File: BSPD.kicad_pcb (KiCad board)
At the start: 2 copper layers, 78.7 x 83 mm, 46 parts, among them J1 Screw_Terminal_3.5mm_2, J2 Screw_Terminal_3.5mm_2, J3 Screw_Terminal_3.5mm_3, J4 Screw_Terminal_3.5mm_3, J5 Screw_Terminal_3.5mm_2, J6 Screw_Terminal_3.5mm_2, J7 Screw_Terminal_3.5mm_2, Q3 NPN, U1 LM358, U2 LM358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

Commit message: Text Added
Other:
- board text added: "BSPD MAMUN_DAQ"
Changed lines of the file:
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@@
 		(layer "Edge.Cuts")
+	)
+	(gr_text "BSPD\nMAMUN_DAQ"
+		(at 186.5 122 0)
+		(layer "B.Cu")
+		(effects
+			(font
+				(size 1.5 1.5)
+				(thickness 0.3)
+				(bold yes)
+			)
+			(justify left bottom mirror)
+		)
 	)
 	(via

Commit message: Rounded PCB
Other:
- board size 78.7 x 83 mm -> 80.9 x 85 mm
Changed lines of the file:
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@@
 		(embedded_fonts no)
 	)
-	(gr_rect
-		(start 115.345 45)
-		(end 194 128)
+	(gr_line
+		(start 126.07107 43)
+		(end 186.92893 43)
 		(stroke
 			(width 0.05)
 			(type default)
 		)
-		(fill no)
 		(layer "Edge.Cuts")
 	)
+	(gr_arc
+		(start 116.071068 53)
+		(mid 119.000001 45.928931)
+		(end 126.07107 43)
+		(stroke
+			(width 0.05)
+			(type default)
+		)
+		(layer "Edge.Cuts")
+	)
+	(gr_arc
+		(start 126 128)
+		(mid 118.928932 125.071068)
+		(end 116 118)
+		(stroke
+			(width 0.05)
+			(type default)
+		)
+		(layer "Edge.Cuts")
+	)
+	(gr_line
+		(start 116 118)
+		(end 116.071068 53)
+		(stroke
+			(width 0.05)
+			(type default)
+		)
+		(layer "Edge.Cuts")
+	)
+	(gr_arc
+		(start 196.928932 117.928932)
+		(mid 194 125)
+		(end 186.928932 127.928932)
+		(stroke
+			(width 0.05)
+			(type default)
+		)
+		(layer "Edge.Cuts")
+	)
+	(gr_line
+		(start 186.928932 127.928932)
+		(end 126 128)
+		(stroke
+			(width 0.05)
+			(type default)
+		)
+		(layer "Edge.Cuts")
+	)
+	(gr_line
+		(start 196.928932 53)
+		(end 196.928932 118)
+		(stroke
+			(width 0.05)
+			(type default)
+		)
+		(layer "Edge.Cuts")
+	)
+	(gr_arc
+		(start 186.928932 43)
+		(mid 194 45.928932)
+		(end 196.928932 53)
+		(stroke
+			(width 0.05)
+			(type default)
+		)
+		(layer "Edge.Cuts")
+	)

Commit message: Final Commit for print
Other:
- board size 80.9 x 85 mm -> 78 x 86 mm
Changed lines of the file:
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@@
 		(embedded_fonts no)
 	)
-	(gr_line
-		(start 126.07107 43)
-		(end 186.92893 43)
+	(gr_rect
+		(start 116 43)
+		(end 194 129)
 		(stroke
 			(width 0.05)
 			(type default)
 		)
+		(fill no)
 		(layer "Edge.Cuts")
 	)
-	(gr_arc
-		(start 116.071068 53)
-		(mid 119.000001 45.928931)
-		(end 126.07107 43)
-		(stroke
-			(width 0.05)
-			(type default)
-		)
-		(layer "Edge.Cuts")
-	)
-	(gr_arc
-		(start 126 128)
-		(mid 118.928932 125.071068)
-		(end 116 118)
-		(stroke
-			(width 0.05)
-			(type default)
-		)
-		(layer "Edge.Cuts")
-	)
-	(gr_line
-		(start 116 118)
-		(end 116.071068 53)
-		(stroke
-			(width 0.05)
-			(type default)
-		)
-		(layer "Edge.Cuts")
-	)
-	(gr_arc
-		(start 196.928932 117.928932)
-		(mid 194 125)
-		(end 186.928932 127.928932)
-		(stroke
-			(width 0.05)
-			(type default)
-		)
-		(layer "Edge.Cuts")
-	)
-	(gr_line
-		(start 186.928932 127.928932)
-		(end 126 128)
-		(stroke
-			(width 0.05)
-			(type default)
-		)
-		(layer "Edge.Cuts")
-	)
-	(gr_line
-		(start 196.928932 53)
-		(end 196.928932 118)
-		(stroke
-			(width 0.05)
-			(type default)
-		)
-		(layer "Edge.Cuts")
-	)
-	(gr_arc
-		(start 186.928932 43)
-		(mid 194 45.928932)
-		(end 196.928932 53)
-		(stroke
-			(width 0.05)
-			(type default)
-		)
-		(layer "Edge.Cuts")
-	)

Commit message: Solid Zone Added
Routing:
- added copper zone on B.Cu, net GND
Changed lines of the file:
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@@
 		(net 24)
+	)
+	(zone
+		(net 2)
+		(net_name "GND")
+		(layer "B.Cu")
+		(hatch edge 0.5)
+		(connect_pads
+			(clearance 0.4)
+		)
+		(min_thickness 0.25)
+		(filled_areas_thickness no)
+		(fill yes
+			(thermal_gap 0.5)
+			(thermal_bridge_width 0.5)
+		)
+		(polygon
+			(pts
+				(xy 113 42) (xy 199 41) (xy 195 136) (xy 95 139)
+			)
+		)
 	)
 	(embedded_fonts no)

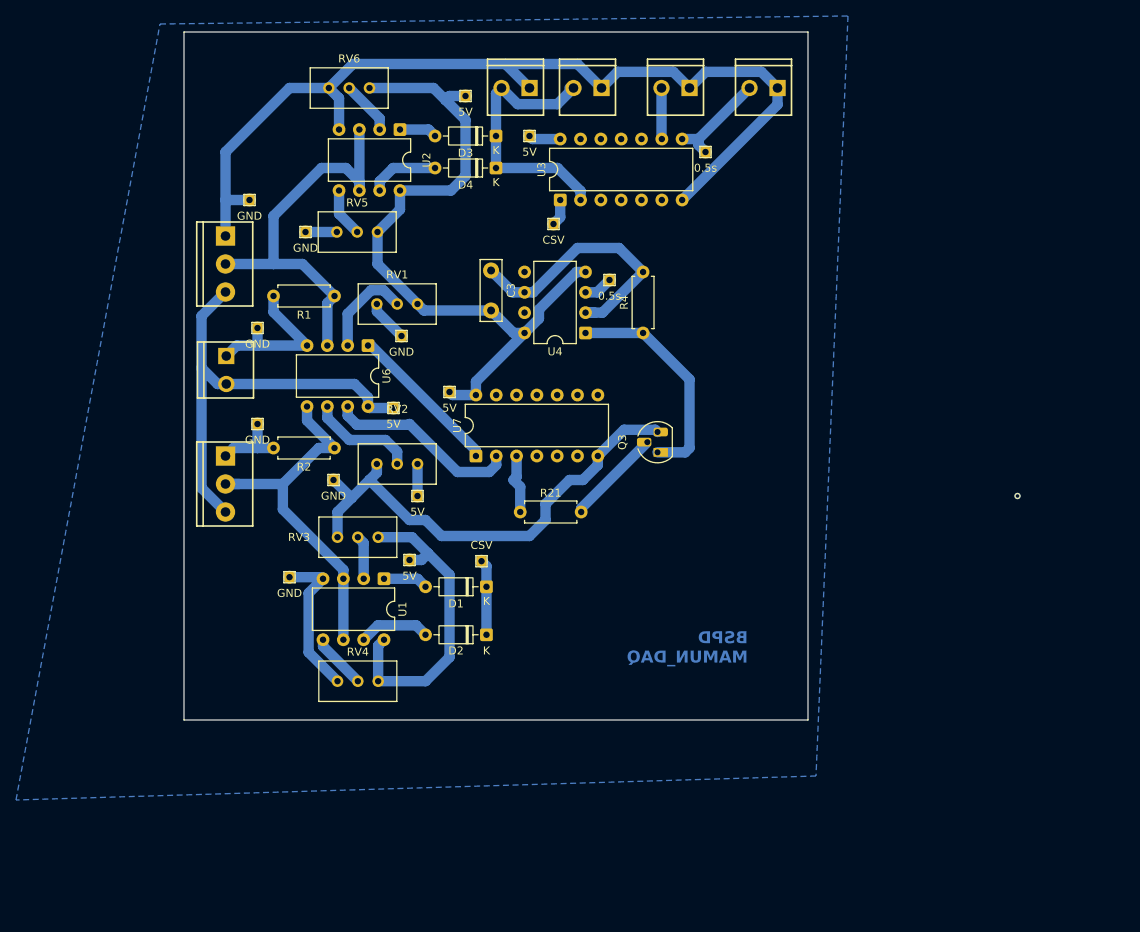
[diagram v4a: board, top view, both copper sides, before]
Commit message: updated pcb with better clearance
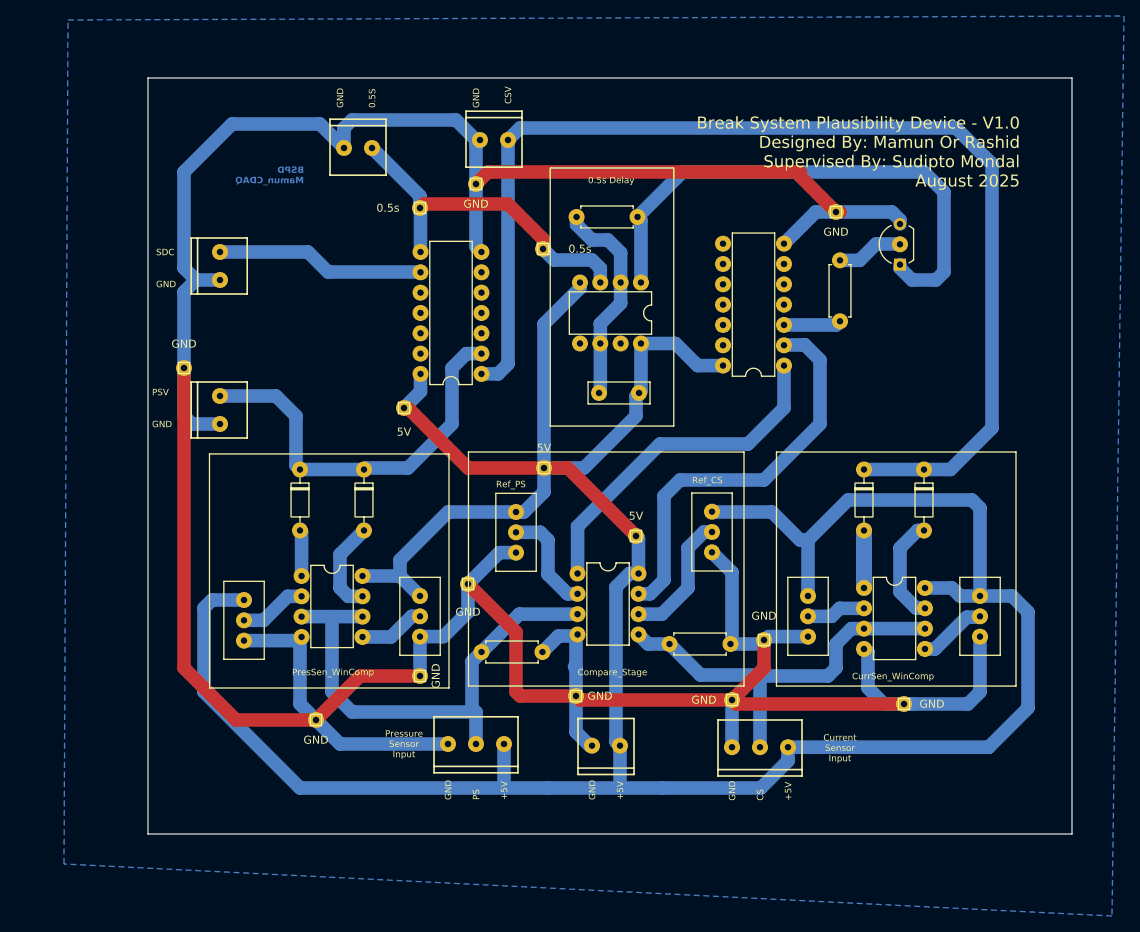
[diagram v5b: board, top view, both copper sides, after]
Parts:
- removed the 5V at (151.2, 51.0)
- removed the 5V at (159.2, 56.0)
- removed the 5V at (144.2, 109.0)
- removed the 5V at (145.2, 101.0)
- removed CSV (x2): TestPoint_THTPad_1.0x1.0mm_Drill0.5mm, TestPoint:TestPoint_THTPad_1.0x1.0mm_Drill0.5mm
- removed the GND at (124.2, 64.0)
- removed the GND at (125.2, 80.0)
- removed the GND at (129.2, 111.2)
- removed the GND at (143.2, 81.0)
- removed the GND at (134.7, 99.0)
- added 5V: TestPoint_THTPad_1.0x1.0mm_Drill0.5mm, TestPoint:TestPoint_THTPad_1.0x1.0mm_Drill0.5mm, F.Cu at (143.5, 90.0)
- added GND: TestPoint_THTPad_1.0x1.0mm_Drill0.5mm, TestPoint:TestPoint_THTPad_1.0x1.0mm_Drill0.5mm, F.Cu at (116.0, 85.0)
- added GND: TestPoint_THTPad_1.0x1.0mm_Drill0.5mm, TestPoint:TestPoint_THTPad_1.0x1.0mm_Drill0.5mm, F.Cu at (152.5, 62.0)
- added GND: TestPoint_THTPad_1.0x1.0mm_Drill0.5mm, TestPoint:TestPoint_THTPad_1.0x1.0mm_Drill0.5mm, F.Cu at (188.5, 119.0)
- added GND: TestPoint_THTPad_1.0x1.0mm_Drill0.5mm, TestPoint:TestPoint_THTPad_1.0x1.0mm_Drill0.5mm, F.Cu at (151.5, 112.0)
- added GND: TestPoint_THTPad_1.0x1.0mm_Drill0.5mm, TestPoint:TestPoint_THTPad_1.0x1.0mm_Drill0.5mm, F.Cu at (197.5, 65.5)
- added GND: TestPoint_THTPad_1.0x1.0mm_Drill0.5mm, TestPoint:TestPoint_THTPad_1.0x1.0mm_Drill0.5mm, F.Cu at (206.0, 127.0)
- added GND: TestPoint_THTPad_1.0x1.0mm_Drill0.5mm, TestPoint:TestPoint_THTPad_1.0x1.0mm_Drill0.5mm, F.Cu at (132.5, 129.0)
- added GND: TestPoint_THTPad_1.0x1.0mm_Drill0.5mm, TestPoint:TestPoint_THTPad_1.0x1.0mm_Drill0.5mm, F.Cu at (165.0, 126.0)
- Q3: footprint Package_TO_SOT_THT:TO-92_HandSolder -> Package_TO_SOT_THT:TO-92L_Inline_Wide
- moved RV4 76.0 mm to (215.5, 113.5), turned to 90 degrees
- moved J3 73.0 mm to (184.5, 132.4), turned to 0 degrees
- moved J4 69.3 mm to (149.0, 132.0), turned to 0 degrees
- moved GND 68.6 mm to (184.5, 126.5), turned to 90 degrees
- moved J7 66.8 mm to (167.0, 132.2), turned to 0 degrees
- moved RV6 65.9 mm to (123.5, 114.0), turned to 90 degrees
- moved J1 62.2 mm to (120.5, 70.5), turned to -90 degrees
- moved J2 61.3 mm to (120.5, 88.5), turned to -90 degrees
- moved U1 60.0 mm to (201.0, 112.5), turned to 0 degrees
- moved D2 58.5 mm to (208.5, 97.7), turned to -90 degrees
- moved GND 57.3 mm to (145.5, 123.5), turned to 90 degrees
- moved U2 57.1 mm to (130.7, 111.0), turned to 0 degrees
- moved RV3 54.2 mm to (194.0, 113.5), turned to 90 degrees
- moved J5 51.2 mm to (139.5, 57.5)
- moved D1 49.4 mm to (201.0, 97.7), turned to -90 degrees
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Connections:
- J1 pad 1: GND -> /SDC
- J1 pad 2: /SDC -> GND
- J2 pad 1: GND -> /Pressure_Sensor_Validated
- J2 pad 2: /Pressure_Sensor_Validated -> GND
- J5 pad 1: GND -> /0.5s_delay
- J5 pad 2: /0.5s_delay -> GND
- J6 pad 1: GND -> /Current_Sensor_Validated
- J6 pad 2: /Pressure_Sensor_Validated -> GND
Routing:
- net GND: track 240.0 -> 446.9 mm
- net +5V: track 194.0 -> 385.2 mm
- net /Current_Sensor_Validated: track 12.8 -> 146.0 mm
- net Net-(Q3-C): track 28.2 -> 67.0 mm
- net /0.5s_delay: track 16.7 -> 44.1 mm
- net /Current_Comp_Out: track 24.2 -> 50.9 mm
- net /Pressure_Comp_Out: track 19.6 -> 43.3 mm
- net /SDC: track 6.40 -> 26.1 mm
- net /Pressure_Sensor_Validated: track 34.3 -> 50.2 mm
- net /Pressure_Sensor: track 50.5 -> 62.0 mm
- net /2: track 34.1 -> 26.6 mm
- net /Current_Sensor: track 46.4 -> 51.2 mm
- net Net-(D2-A): track 8.97 -> 13.6 mm
- net Net-(Q3-B): track 11.9 -> 8.40 mm
- net Net-(U6B--): track 13.4 -> 16.4 mm
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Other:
- board size 78 x 86 mm -> 115.5 x 94.5 mm
- board text added: "+5V"
- board text added: "0.5S"
- board text added: "0.5s Delay"
- board text added: "BSPD Mamun_CDAQ"
- board text added: "Break System Plausibility Device - V1.0 Designed By: Mamun Or Rashid Supervised By: Sudipto Mondal August 2025"
- board text added: "CS"
- board text added: "CSV"
- board text added: "Compare_Stage"
- board text added: "CurrSen_WinComp"
- board text added: "Current Sensor Input"
- board text added: "GND"
- board text added: "PS"
- board text added: "PSV"
- board text added: "PresSen_WinComp"
- board text added: "Pressure Sensor Input"
- board text added: "Ref_CS"
- board text added: "Ref_PS"
- board text added: "SDC"
- board text removed: "BSPD MAMUN_DAQ"
